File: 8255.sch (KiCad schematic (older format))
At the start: 4 parts

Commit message: Merged 8254
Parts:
- gave numbers to parts that had none: 1
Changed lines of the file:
@@
 $Descr A4 8268 11693 portrait
 encoding utf-8
-Sheet 4 6
+Sheet 3 8
 Title ""
 Date ""
@@
 $EndDescr
 $Comp
-L power:GND #PWR?
+L power:GND #PWR0119
 U 1 1 623E01E4
 P 2100 6700
-F 0 "#PWR?" H 2100 6450 50  0001 C CNN
+F 0 "#PWR0119" H 2100 6450 50  0001 C CNN
 F 1 "GND" V 2105 6572 50  0000 R CNN
 F 2 "" H 2100 6700 50  0001 C CNN
@@
 $EndComp
 $Comp
-L power:+5V #PWR?
+L power:+5V #PWR0120
 U 1 1 623E01DA
 P 2100 3500
-F 0 "#PWR?" H 2100 3350 50  0001 C CNN
+F 0 "#PWR0120" H 2100 3350 50  0001 C CNN
 F 1 "+5V" V 2115 3628 50  0000 L CNN
 F 2 "" H 2100 3500 50  0001 C CNN
@@
 $EndComp
 $Comp
-L power:GND #PWR?
+L power:GND #PWR0121
 U 1 1 623E22CF
 P 5300 10850
-F 0 "#PWR?" H 5300 10600 50  0001 C CNN
+F 0 "#PWR0121" H 5300 10600 50  0001 C CNN
 F 1 "GND" V 5305 10722 50  0000 R CNN
 F 2 "" H 5300 10850 50  0001 C CNN
@@
 $EndComp
 $Comp
-L power:+5V #PWR?
+L power:+5V #PWR0122
 U 1 1 6248CB5B
 P 4400 3500
-F 0 "#PWR?" H 4400 3350 50  0001 C CNN
+F 0 "#PWR0122" H 4400 3350 50  0001 C CNN
 F 1 "+5V" V 4415 3628 50  0000 L CNN
 F 2 "" H 4400 3500 50  0001 C CNN
@@
 $EndComp
 $Comp
-L power:GND #PWR?
+L power:GND #PWR0123
 U 1 1 6248CB55
 P 4400 6700
-F 0 "#PWR?" H 4400 6450 50  0001 C CNN
+F 0 "#PWR0123" H 4400 6450 50  0001 C CNN
 F 1 "GND" V 4405 6572 50  0000 R CNN
 F 2 "" H 4400 6700 50  0001 C CNN
@@
 $EndComp
 $Comp
-L power:GND #PWR?
+L power:GND #PWR0124
 U 1 1 624D64B0
 P 6600 6700
-F 0 "#PWR?" H 6600 6450 50  0001 C CNN
+F 0 "#PWR0124" H 6600 6450 50  0001 C CNN
 F 1 "GND" V 6605 6572 50  0000 R CNN
 F 2 "" H 6600 6700 50  0001 C CNN
@@
 $EndComp
 $Comp
-L power:+5V #PWR?
+L power:+5V #PWR0125
 U 1 1 624D64B6
 P 6600 3500
-F 0 "#PWR?" H 6600 3350 50  0001 C CNN
+F 0 "#PWR0125" H 6600 3350 50  0001 C CNN
 F 1 "+5V" V 6615 3628 50  0000 L CNN
 F 2 "" H 6600 3500 50  0001 C CNN
@@
 	5700 4900 5600 4900
 $Comp
-L Logic_Programmable:PAL16L8 U?
+L Logic_Programmable:PAL16L8 U8
 U 1 1 62400DDA
 P 2200 2200
-F 0 "U?" H 2200 3081 50  0000 C CNN
+F 0 "U8" H 2200 3081 50  0000 C CNN
 F 1 "PAL16L8" H 2200 2990 50  0000 C CNN
 F 2 "" H 2200 2200 50  0001 C CNN
@@
 	1500 3400 2900 3400
 $Comp
-L power:+5V #PWR?
+L power:+5V #PWR0126
 U 1 1 62829F92
 P 2200 1500
-F 0 "#PWR?" H 2200 1350 50  0001 C CNN
+F 0 "#PWR0126" H 2200 1350 50  0001 C CNN
 F 1 "+5V" V 2215 1628 50  0000 L CNN
 F 2 "" H 2200 1500 50  0001 C CNN
@@
 $EndComp
 $Comp
-L power:GND #PWR?
+L power:GND #PWR0127
 U 1 1 6282AC0F
 P 2200 2800
-F 0 "#PWR?" H 2200 2550 50  0001 C CNN
+F 0 "#PWR0127" H 2200 2550 50  0001 C CNN
 F 1 "GND" H 2205 2627 50  0000 C CNN
 F 2 "" H 2200 2800 50  0001 C CNN

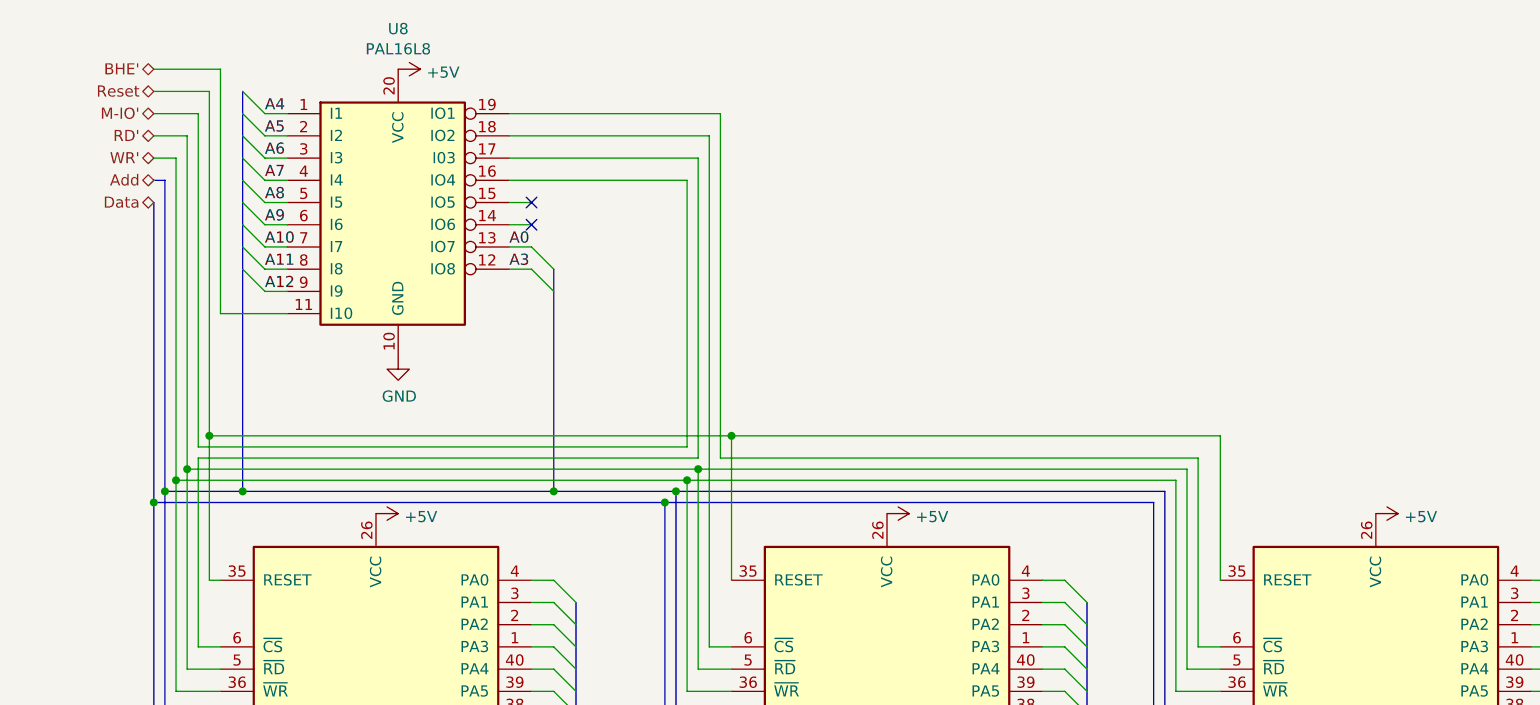
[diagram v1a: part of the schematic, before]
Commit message: Integrated LCD.  Fixed issues with busses
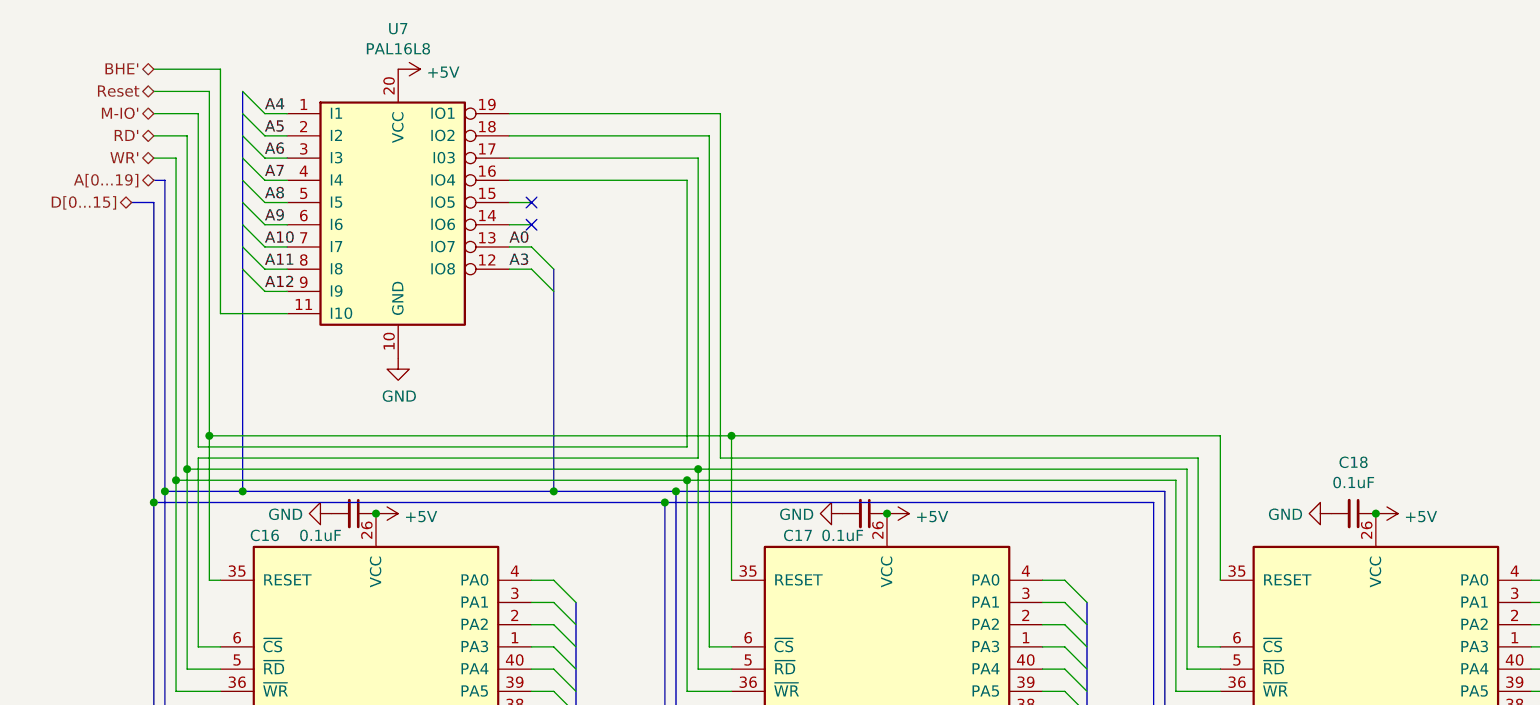
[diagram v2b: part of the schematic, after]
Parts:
- added C16, C17, C18: 0.1uF, symbol Device:C_Small
- renumbered U8 to U7
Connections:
- net +5V: now also C16.1, C17.1, C18.1
- net GND: now also C16.2, C17.2, C18.2
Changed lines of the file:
@@
 $Descr A4 8268 11693 portrait
 encoding utf-8
-Sheet 3 8
+Sheet 3 9
 Title ""
 Date ""
@@
 $EndDescr
 $Comp
-L power:GND #PWR0119
+L power:GND #PWR021
 U 1 1 623E01E4
 P 2100 6700
-F 0 "#PWR0119" H 2100 6450 50  0001 C CNN
+F 0 "#PWR021" H 2100 6450 50  0001 C CNN
 F 1 "GND" V 2105 6572 50  0000 R CNN
 F 2 "" H 2100 6700 50  0001 C CNN
@@
 $EndComp
 $Comp
-L power:+5V #PWR0120
+L power:+5V #PWR020
 U 1 1 623E01DA
 P 2100 3500
-F 0 "#PWR0120" H 2100 3350 50  0001 C CNN
+F 0 "#PWR020" H 2100 3350 50  0001 C CNN
 F 1 "+5V" V 2115 3628 50  0000 L CNN
 F 2 "" H 2100 3500 50  0001 C CNN
@@
 $EndComp
 $Comp
-L power:GND #PWR0121
+L power:GND #PWR026
 U 1 1 623E22CF
 P 5300 10850
-F 0 "#PWR0121" H 5300 10600 50  0001 C CNN
+F 0 "#PWR026" H 5300 10600 50  0001 C CNN
 F 1 "GND" V 5305 10722 50  0000 R CNN
 F 2 "" H 5300 10850 50  0001 C CNN
@@
 $EndComp
 $Comp
-L power:+5V #PWR0122
+L power:+5V #PWR024
 U 1 1 6248CB5B
 P 4400 3500
-F 0 "#PWR0122" H 4400 3350 50  0001 C CNN
+F 0 "#PWR024" H 4400 3350 50  0001 C CNN
 F 1 "+5V" V 4415 3628 50  0000 L CNN
 F 2 "" H 4400 3500 50  0001 C CNN
@@
 $EndComp
 $Comp
-L power:GND #PWR0123
+L power:GND #PWR025
 U 1 1 6248CB55
 P 4400 6700
-F 0 "#PWR0123" H 4400 6450 50  0001 C CNN
+F 0 "#PWR025" H 4400 6450 50  0001 C CNN
 F 1 "GND" V 4405 6572 50  0000 R CNN
 F 2 "" H 4400 6700 50  0001 C CNN
@@
 $EndComp
 $Comp
-L power:GND #PWR0124
+L power:GND #PWR028
 U 1 1 624D64B0
 P 6600 6700
-F 0 "#PWR0124" H 6600 6450 50  0001 C CNN
+F 0 "#PWR028" H 6600 6450 50  0001 C CNN
 F 1 "GND" V 6605 6572 50  0000 R CNN
 F 2 "" H 6600 6700 50  0001 C CNN
@@
 $EndComp
 $Comp
-L power:+5V #PWR0125
+L power:+5V #PWR027
 U 1 1 624D64B6
 P 6600 3500
-F 0 "#PWR0125" H 6600 3350 50  0001 C CNN
+F 0 "#PWR027" H 6600 3350 50  0001 C CNN
 F 1 "+5V" V 6615 3628 50  0000 L CNN
 F 2 "" H 6600 3500 50  0001 C CNN
@@
 Entry Wire Line
 	5700 4500 5800 4600
-Entry Wire Line
-	5700 4600 5800 4700
 Wire Bus Line
 	5700 4500 5700 4600
@@
 	5700 4900 5600 4900
 $Comp
-L Logic_Programmable:PAL16L8 U8
+L Logic_Programmable:PAL16L8 U7
 U 1 1 62400DDA
 P 2200 2200
-F 0 "U8" H 2200 3081 50  0000 C CNN
+F 0 "U7" H 2200 3081 50  0000 C CNN
 F 1 "PAL16L8" H 2200 2990 50  0000 C CNN
 F 2 "" H 2200 2200 50  0001 C CNN
@@
 	1100 3450 1100 2100
 Connection ~ 1100 3450
-Text HLabel 1100 2100 0    50   BiDi ~ 0
-Data
 Wire Bus Line
 	1150 3400 1150 2000
 Connection ~ 1150 3400
 Text HLabel 1100 2000 0    50   BiDi ~ 0
-Add
+A[0...19]
 Wire Bus Line
 	1150 2000 1100 2000
@@
 	1500 3400 2900 3400
 $Comp
-L power:+5V #PWR0126
+L power:+5V #PWR022
 U 1 1 62829F92
 P 2200 1500
-F 0 "#PWR0126" H 2200 1350 50  0001 C CNN
+F 0 "#PWR022" H 2200 1350 50  0001 C CNN
 F 1 "+5V" V 2215 1628 50  0000 L CNN
 F 2 "" H 2200 1500 50  0001 C CNN
@@
 $EndComp
 $Comp
-L power:GND #PWR0127
+L power:GND #PWR023
 U 1 1 6282AC0F
 P 2200 2800
-F 0 "#PWR0127" H 2200 2550 50  0001 C CNN
+F 0 "#PWR023" H 2200 2550 50  0001 C CNN
 F 1 "GND" H 2205 2627 50  0000 C CNN
 F 2 "" H 2200 2800 50  0001 C CNN
@@
 Text Label 1300 5700 0    50   ~ 0
 D15
-Text Label 3600 5000 0    50   ~ 0
-D0
 Text Label 3600 5100 0    50   ~ 0
 D1
@@
 Text HLabel 7500 6800 0    50   BiDi ~ 0
 PPI3C
+Entry Wire Line
+	5700 4600 5800 4700
+Text Label 3600 5000 0    50   ~ 0
+D0
+Text HLabel 1000 2100 0    50   BiDi ~ 0
+D[0...15]
+Wire Bus Line
+	1100 2100 1000 2100
+$Comp
+L Device:C_Small C17
+U 1 1 61D1B884
+P 4300 3500
+F 0 "C17" V 4400 3200 50  0000 C CNN
+F 1 "0.1uF" V 4400 3400 50  0000 C CNN
+F 2 "" H 4300 3500 50  0001 C CNN
+F 3 "~" H 4300 3500 50  0001 C CNN
+	1    4300 3500
+	0    1    1    0
+$EndComp
+Connection ~ 4400 3500
+$Comp
+L power:GND #PWR0101
+U 1 1 61D1BF8B
+P 4200 3500
+F 0 "#PWR0101" H 4200 3250 50  0001 C CNN
+F 1 "GND" V 4205 3372 50  0000 R CNN
+F 2 "" H 4200 3500 50  0001 C CNN
+F 3 "" H 4200 3500 50  0001 C CNN
+	1    4200 3500
+	0    1    1    0
+$EndComp
+$Comp
+L Device:C_Small C16
+U 1 1 61D1CE15
+P 2000 3500
+F 0 "C16" V 2100 3100 50  0000 C CNN
+F 1 "0.1uF" V 2100 3350 50  0000 C CNN
+F 2 "" H 2000 3500 50  0001 C CNN
+F 3 "~" H 2000 3500 50  0001 C CNN
+	1    2000 3500
+	0    1    1    0
+$EndComp
+Connection ~ 2100 3500
+$Comp
+L power:GND #PWR0102
+U 1 1 61D1D60F
+P 1900 3500
+F 0 "#PWR0102" H 1900 3250 50  0001 C CNN
+F 1 "GND" V 1905 3372 50  0000 R CNN
+F 2 "" H 1900 3500 50  0001 C CNN
+F 3 "" H 1900 3500 50  0001 C CNN
+	1    1900 3500
+	0    1    1    0
+$EndComp
+$Comp
+L Device:C_Small C18
+U 1 1 61D1DB91
+P 6500 3500
+F 0 "C18" V 6271 3500 50  0000 C CNN
+F 1 "0.1uF" V 6362 3500 50  0000 C CNN
+F 2 "" H 6500 3500 50  0001 C CNN
+F 3 "~" H 6500 3500 50  0001 C CNN
+	1    6500 3500
+	0    1    1    0
+$EndComp
+Connection ~ 6600 3500
+$Comp
+L power:GND #PWR0103
+U 1 1 61D1E103
+P 6400 3500
+F 0 "#PWR0103" H 6400 3250 50  0001 C CNN
+F 1 "GND" V 6405 3372 50  0000 R CNN
+F 2 "" H 6400 3500 50  0001 C CNN
+F 3 "" H 6400 3500 50  0001 C CNN
+	1    6400 3500
+	0    1    1    0
+$EndComp
 Wire Bus Line
 	2900 2400 2900 3400
@@
 	7500 5700 7500 6600
 Wire Bus Line
+	5300 5700 5300 6800
+Wire Bus Line
 	3000 5700 3000 6800
-Wire Bus Line
-	5300 5700 5300 6800
 $EndSCHEMATC

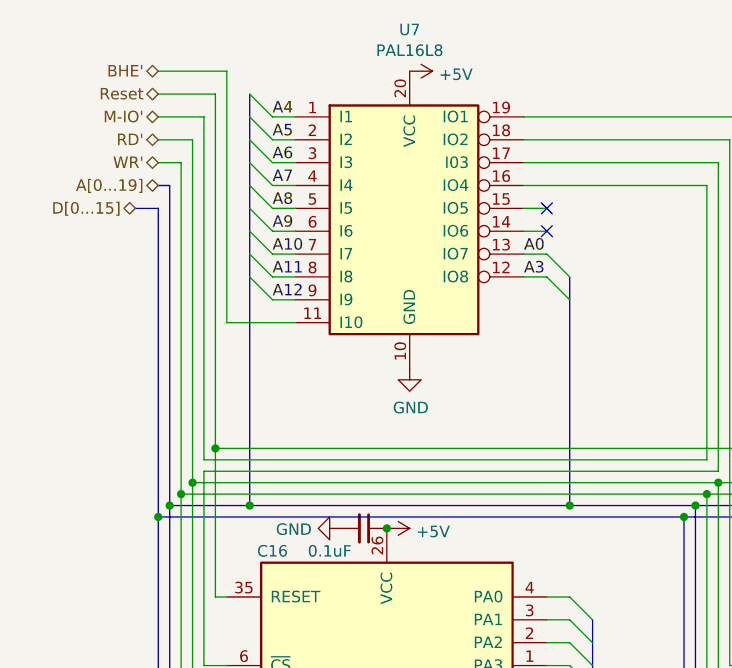
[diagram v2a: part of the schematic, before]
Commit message: All schematics present
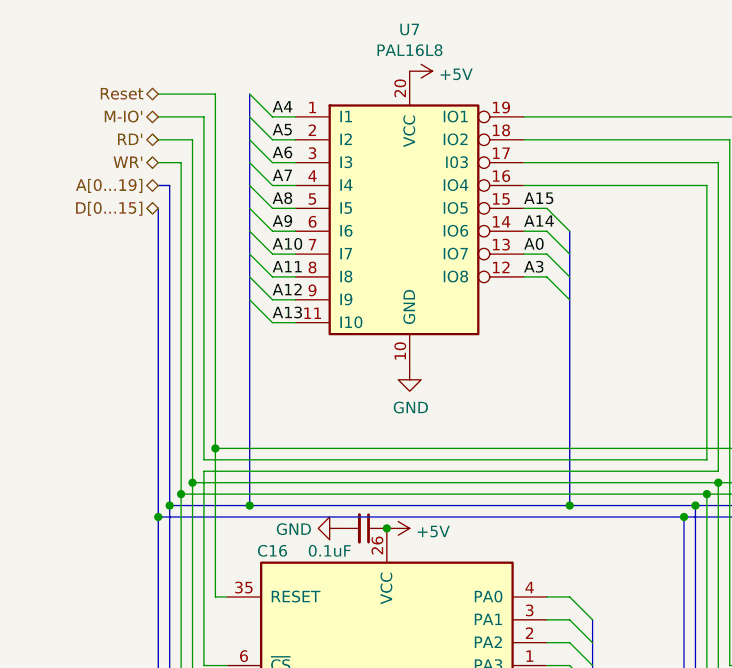
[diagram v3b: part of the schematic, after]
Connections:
- net A14: now reaches U7.14 (IO6)
- net A15: now reaches U7.15 (IO5)
- net BHE' renamed A13
- no-connect marks 2 -> 0
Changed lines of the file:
@@
 $Descr A4 8268 11693 portrait
 encoding utf-8
-Sheet 3 9
+Sheet 3 12
 Title ""
 Date ""
@@
 Text Label 2700 2300 0    50   ~ 0
 A0
-NoConn ~ 2800 2100
-NoConn ~ 2800 2200
 Wire Wire Line
 	1350 3800 1400 3800
-Text HLabel 1100 1500 0    50   BiDi ~ 0
-BHE'
-Wire Wire Line
-	1400 2600 1400 1500
-Wire Wire Line
-	1400 1500 1100 1500
-Wire Wire Line
-	1400 2600 1700 2600
 Text Label 1300 5000 0    50   ~ 0
 D8
@@
 Text Label 3600 5000 0    50   ~ 0
 D0
-Text HLabel 1000 2100 0    50   BiDi ~ 0
+Text HLabel 1100 2100 0    50   BiDi ~ 0
 D[0...15]
-Wire Bus Line
-	1100 2100 1000 2100
 $Comp
 L Device:C_Small C17
@@
 	0    1    1    0
 $EndComp
-Wire Bus Line
-	2900 2400 2900 3400
+Entry Wire Line
+	1500 2500 1600 2600
+Wire Wire Line
+	1600 2600 1700 2600
+Entry Wire Line
+	2800 2100 2900 2200
+Entry Wire Line
+	2800 2200 2900 2300
+Text Label 1600 2600 0    50   ~ 0
+A13
+Text Label 2700 2200 0    50   ~ 0
+A14
+Text Label 2700 2100 0    50   ~ 0
+A15
+Wire Bus Line
+	2900 2200 2900 3400
 Wire Bus Line
 	1200 4900 1200 5600

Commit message: Started PCB
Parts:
- added J10, J11, J12, J13, J5, J6, J7, J8, J9: Conn_01x08, Connector:Banana_Jack_1Pin, symbol Connector_Generic:Conn_01x08
- C3: renamed from C16; footprint (none) -> Capacitor_SMD:CP_Elec_3x5.3
- C4: renamed from C17; footprint (none) -> Capacitor_SMD:CP_Elec_3x5.3
- C5: renamed from C18; footprint (none) -> Capacitor_SMD:CP_Elec_3x5.3
- U7: footprint (none) -> Package_DIP:DIP-20_W7.62mm
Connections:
- net at PPI1.1 (PA3): now also J5.4 (Pin_4)
- net at PPI1.10 (PC7): now also J7.8 (Pin_8)
- net at PPI1.11 (PC6): now also J7.7 (Pin_7)
- net at PPI1.12 (PC5): now also J7.6 (Pin_6)
- net at PPI1.13 (PC4): now also J7.5 (Pin_5)
- net at PPI1.14 (PC0): now also J7.1 (Pin_1)
- net at PPI1.15 (PC1): now also J7.2 (Pin_2)
- net at PPI1.16 (PC2): now also J7.3 (Pin_3)
- net at PPI1.17 (PC3): now also J7.4 (Pin_4)
- net at PPI1.18 (PB0): now also J6.1 (Pin_1)
- net at PPI1.19 (PB1): now also J6.2 (Pin_2)
- net at PPI1.2 (PA2): now also J5.3 (Pin_3)
- net at PPI1.20 (PB2): now also J6.3 (Pin_3)
- net at PPI1.21 (PB3): now also J6.4 (Pin_4)
- net at PPI1.22 (PB4): now also J6.5 (Pin_5)
- net at PPI1.23 (PB5): now also J6.6 (Pin_6)
- net at PPI1.24 (PB6): now also J6.7 (Pin_7)
- net at PPI1.25 (PB7): now also J6.8 (Pin_8)
- net at PPI1.3 (PA1): now also J5.2 (Pin_2)
- net at PPI1.37 (PA7): now also J5.8 (Pin_8)
- net at PPI1.38 (PA6): now also J5.7 (Pin_7)
- net at PPI1.39 (PA5): now also J5.6 (Pin_6)
- net at PPI1.4 (PA0): now also J5.1 (Pin_1)
- net at PPI1.40 (PA4): now also J5.5 (Pin_5)
- net at PPI2.1 (PA3): now also J8.4 (Pin_4)
- net at PPI2.10 (PC7): now also J10.8 (Pin_8)
- net at PPI2.11 (PC6): now also J10.7 (Pin_7)
- net at PPI2.12 (PC5): now also J10.6 (Pin_6)
- net at PPI2.13 (PC4): now also J10.5 (Pin_5)
- net at PPI2.14 (PC0): now also J10.1 (Pin_1)
- net at PPI2.15 (PC1): now also J10.2 (Pin_2)
- net at PPI2.16 (PC2): now also J10.3 (Pin_3)
- net at PPI2.17 (PC3): now also J10.4 (Pin_4)
- net at PPI2.18 (PB0): now also J9.1 (Pin_1)
- net at PPI2.19 (PB1): now also J9.2 (Pin_2)
- net at PPI2.2 (PA2): now also J8.3 (Pin_3)
- net at PPI2.20 (PB2): now also J9.3 (Pin_3)
- net at PPI2.21 (PB3): now also J9.4 (Pin_4)
- net at PPI2.22 (PB4): now also J9.5 (Pin_5)
- net at PPI2.23 (PB5): now also J9.6 (Pin_6)
- net at PPI2.24 (PB6): now also J9.7 (Pin_7)
- net at PPI2.25 (PB7): now also J9.8 (Pin_8)
- net at PPI2.3 (PA1): now also J8.2 (Pin_2)
- net at PPI2.37 (PA7): now also J8.8 (Pin_8)
- net at PPI2.38 (PA6): now also J8.7 (Pin_7)
- net at PPI2.39 (PA5): now also J8.6 (Pin_6)
- net at PPI2.4 (PA0): now also J8.1 (Pin_1)
- net at PPI2.40 (PA4): now also J8.5 (Pin_5)
- net at PPI3.1 (PA3): now also J11.4 (Pin_4)
- net at PPI3.10 (PC7): now also J12.8 (Pin_8)
- net at PPI3.11 (PC6): now also J12.7 (Pin_7)
- net at PPI3.12 (PC5): now also J12.6 (Pin_6)
- net at PPI3.13 (PC4): now also J12.5 (Pin_5)
- net at PPI3.14 (PC0): now also J12.1 (Pin_1)
- net at PPI3.15 (PC1): now also J12.2 (Pin_2)
- net at PPI3.16 (PC2): now also J12.3 (Pin_3)
- net at PPI3.17 (PC3): now also J12.4 (Pin_4)
- net at PPI3.18 (PB0): now also J13.1 (Pin_1)
- net at PPI3.19 (PB1): now also J13.2 (Pin_2)
- net at PPI3.2 (PA2): now also J11.3 (Pin_3)
- net at PPI3.20 (PB2): now also J13.3 (Pin_3)
- net at PPI3.21 (PB3): now also J13.4 (Pin_4)
- net at PPI3.22 (PB4): now also J13.5 (Pin_5)
- net at PPI3.23 (PB5): now also J13.6 (Pin_6)
- net at PPI3.24 (PB6): now also J13.7 (Pin_7)
- net at PPI3.25 (PB7): now also J13.8 (Pin_8)
- net at PPI3.3 (PA1): now also J11.2 (Pin_2)
- net at PPI3.37 (PA7): now also J11.8 (Pin_8)
- net at PPI3.38 (PA6): now also J11.7 (Pin_7)
- net at PPI3.39 (PA5): now also J11.6 (Pin_6)
- net at PPI3.4 (PA0): now also J11.1 (Pin_1)
- net at PPI3.40 (PA4): now also J11.5 (Pin_5)
